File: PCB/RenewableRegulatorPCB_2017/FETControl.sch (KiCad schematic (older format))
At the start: 10 parts, among them Q1 TK32A12N1, U1 IR2117

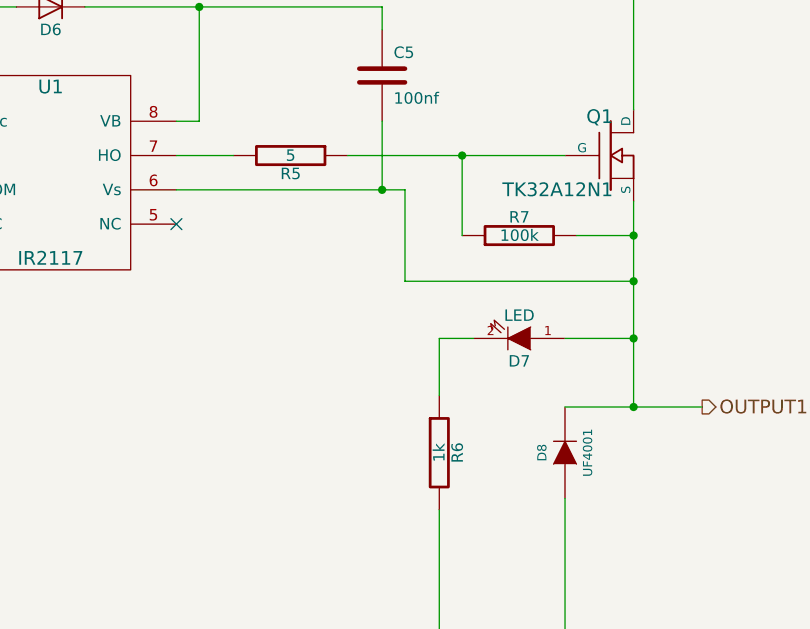
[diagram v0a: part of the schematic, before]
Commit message: Moved code into new file structure
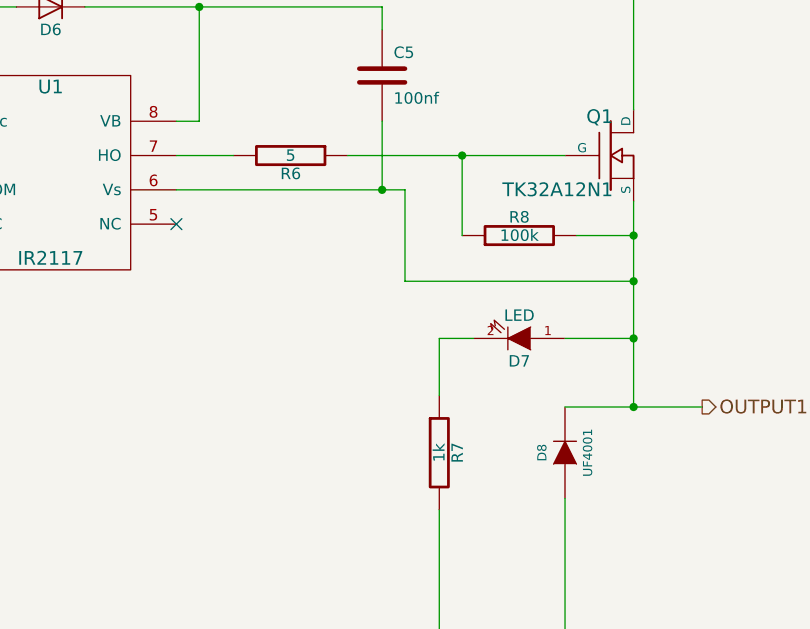
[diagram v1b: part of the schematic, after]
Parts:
- renumbered R5 to R6, R6 to R7, R7 to R8
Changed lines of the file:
@@
 $EndComp
 $Comp
-L R-RESCUE-RenewableRegulatorPCB_2017 R7
+L R-RESCUE-RenewableRegulatorPCB_2017 R8
 U 1 1 538B0FED
 P 6300 3500
-F 0 "R7" V 6380 3500 50  0000 C CNN
+F 0 "R8" V 6380 3500 50  0000 C CNN
 F 1 "100k" V 6300 3500 50  0000 C CNN
 F 2 "REInnovationFootprint:TH_Resistor_1" H 6300 3500 60  0001 C CNN
@@
 $EndComp
 $Comp
-L R-RESCUE-RenewableRegulatorPCB_2017 R6
+L R-RESCUE-RenewableRegulatorPCB_2017 R7
 U 1 1 538B100B
 P 5950 4450
-F 0 "R6" V 6030 4450 50  0000 C CNN
+F 0 "R7" V 6030 4450 50  0000 C CNN
 F 1 "1k" V 5950 4450 50  0000 C CNN
 F 2 "REInnovationFootprint:TH_Resistor_1" H 5950 4450 60  0001 C CNN
@@
 	4900 3000 4800 3000
 $Comp
-L R-RESCUE-RenewableRegulatorPCB_2017 R5
+L R-RESCUE-RenewableRegulatorPCB_2017 R6
 U 1 1 58E36FBB
 P 5300 3150
-F 0 "R5" V 5380 3150 50  0000 C CNN
+F 0 "R6" V 5380 3150 50  0000 C CNN
 F 1 "5" V 5300 3150 50  0000 C CNN
 F 2 "REInnovationFootprint:TH_Resistor_1" H 5300 3150 60  0001 C CNN

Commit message: Large update of PCB design
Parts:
- added P10: TP_FET, matts_components:1pin_0_8mm, symbol CONN_01X01
- D6: Description (none) -> Schottky Diode >1A; Manufacturer (none) -> HY Electronic Corp; Manufacturer Part No (none) -> 1N5822; Supplier 1 (none) -> RS; Supplier 1 Cost (none) -> 0.045; Supplier 1 Part No (none) -> 917-9102
- D7: Supplier 1 Cost (none) -> 0.1
- D8: value UF4001 -> UF4002; Description (none) -> Fast rectifier for Flyback. 100V; Manufacturer (none) -> Vishay; Manufacturer Part No (none) -> UF4002-E3; Supplier 1 (none) -> RS; Supplier 1 Cost (none) -> 0.12; Supplier 1 Part No (none) -> 628-9732
- U1: Description (none) -> High Voltage High Side FET driver; Manufacturer (none) -> Infineon; Manufacturer Part No (none) -> IR2117PBF; Supplier 1 (none) -> RS; Supplier 1 Cost (none) -> 1.76; Supplier 1 Part No (none) -> 540-9711; Supplier 2 (none) -> DigiKey
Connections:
- net at Q1.G, R6.1, R8.1: now also P10.1 (P1)
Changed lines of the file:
@@
 F 2 "REInnovationFootprint:TH_LED-5MM_larg_pad" H 6300 3950 60  0001 C CNN
 F 3 "" H 6300 3950 60  0000 C CNN
+F 4 "~" H 6300 3950 60  0000 C CNN "Notes"
+F 5 "~" H 6300 3950 60  0001 C CNN "Description"
+F 6 "~" H 6300 3950 60  0001 C CNN "Manufacturer"
+F 7 "~" H 6300 3950 60  0001 C CNN "Manufacturer Part No"
+F 8 "~" H 6300 3950 60  0001 C CNN "Supplier 1"
+F 9 "~" H 6300 3950 60  0001 C CNN "Supplier 1 Part No"
+F 10 "0.1" H 6300 3950 60  0001 C CNN "Supplier 1 Cost"
+F 11 "~" H 6300 3950 60  0001 C CNN "Supplier 2"
+F 12 "~" H 6300 3950 60  0001 C CNN "Supplier 2 Part No"
+F 13 "~" H 6300 3950 60  0001 C CNN "Supplier 2 Cost"
 	1    6300 3950
 	-1   0    0    1
@@
 P 6500 4450
 F 0 "D8" H 6500 4550 40  0000 C CNN
-F 1 "UF4001" H 6500 4350 40  0000 C CNN
+F 1 "UF4002" H 6500 4350 40  0000 C CNN
 F 2 "REInnovationFootprint:TH_Diode_1" H 6500 4450 60  0001 C CNN
-F 3 "" H 6500 4450 60  0000 C CNN
+F 3 "http://docs-europe.electrocomponents.com/webdocs/12cf/0900766b812cffe7.pdf" H 6500 4450 60  0001 C CNN
+F 4 "~" H 6500 4450 60  0000 C CNN "Notes"
+F 5 "Fast rectifier for Flyback. 100V" H 6500 4450 60  0001 C CNN "Description"
+F 6 "Vishay" H 6500 4450 60  0001 C CNN "Manufacturer"
+F 7 "UF4002-E3" H 6500 4450 60  0001 C CNN "Manufacturer Part No"
+F 8 "RS" H 6500 4450 60  0001 C CNN "Supplier 1"
+F 9 "628-9732" H 6500 4450 60  0001 C CNN "Supplier 1 Part No"
+F 10 "0.12" H 6500 4450 60  0001 C CNN "Supplier 1 Cost"
+F 11 "~" H 6500 4450 60  0001 C CNN "Supplier 2"
+F 12 "~" H 6500 4450 60  0001 C CNN "Supplier 2 Part No"
+F 13 "~" H 6500 4450 60  0001 C CNN "Supplier 2 Cost"
 	1    6500 4450
 	0    -1   -1   0
@@
 F 1 "IR2117" H 4250 2800 60  0000 C CNN
 F 2 "REInnovationFootprint:DIP-8_300_ELL" H 4800 3300 60  0001 C CNN
-F 3 "" H 4800 3300 60  0000 C CNN
+F 3 "http://www.infineon.com/dgdl/ir2117.pdf?fileId=5546d462533600a4015355c84331168d" H 4800 3300 60  0001 C CNN
+F 4 "~" H 4250 3200 60  0000 C CNN "Notes"
+F 5 "High Voltage High Side FET driver" H 4250 3200 60  0001 C CNN "Description"
+F 6 "Infineon" H 4250 3200 60  0001 C CNN "Manufacturer"
+F 7 "IR2117PBF" H 4250 3200 60  0001 C CNN "Manufacturer Part No"
+F 8 "RS" H 4250 3200 60  0001 C CNN "Supplier 1"
+F 9 "540-9711" H 4250 3200 60  0001 C CNN "Supplier 1 Part No"
+F 10 "1.76" H 4250 3200 60  0001 C CNN "Supplier 1 Cost"
+F 11 "DigiKey" H 4250 3200 60  0001 C CNN "Supplier 2"
+F 12 "~" H 4250 3200 60  0001 C CNN "Supplier 2 Part No"
+F 13 "~" H 4250 3200 60  0001 C CNN "Supplier 2 Cost"
 	1    4250 3200
 	1    0    0    -1
@@
 F 1 "1N5822" H 4250 2400 50  0000 C CNN
 F 2 "REInnovationFootprint:TH_Diode_1" H 4250 2500 50  0001 C CNN
-F 3 "" H 4250 2500 50  0000 C CNN
+F 3 "http://docs-europe.electrocomponents.com/webdocs/14bb/0900766b814bbef7.pdf" H 4250 2500 50  0001 C CNN
+F 4 "~" H 4250 2500 60  0000 C CNN "Notes"
+F 5 "Schottky Diode >1A" H 4250 2500 60  0001 C CNN "Description"
+F 6 "HY Electronic Corp" H 4250 2500 60  0001 C CNN "Manufacturer"
+F 7 "1N5822" H 4250 2500 60  0001 C CNN "Manufacturer Part No"
+F 8 "RS" H 4250 2500 60  0001 C CNN "Supplier 1"
+F 9 "917-9102" H 4250 2500 60  0001 C CNN "Supplier 1 Part No"
+F 10 "0.045" H 4250 2500 60  0001 C CNN "Supplier 1 Cost"
+F 11 "~" H 4250 2500 60  0001 C CNN "Supplier 2"
+F 12 "~" H 4250 2500 60  0001 C CNN "Supplier 2 Part No"
+F 13 "~" H 4250 2500 60  0001 C CNN "Supplier 2 Cost"
 	1    4250 2500
 	-1   0    0    1
@@
 NoConn ~ 4800 3450
 NoConn ~ 3700 3450
+$Comp
+L CONN_01X01 P10
+U 1 1 58E51C3D
+P 6300 2750
+F 0 "P10" H 6300 2850 50  0000 C CNN
+F 1 "TP_FET" V 6400 2750 50  0000 C CNN
+F 2 "matts_components:1pin_0_8mm" H 6300 2750 50  0001 C CNN
+F 3 "" H 6300 2750 50  0000 C CNN
+	1    6300 2750
+	0    -1   -1   0
+$EndComp
+Wire Wire Line
+	6300 2950 6300 3150
+Connection ~ 6300 3150
 $EndSCHEMATC
